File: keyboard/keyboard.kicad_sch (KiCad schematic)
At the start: 200 parts

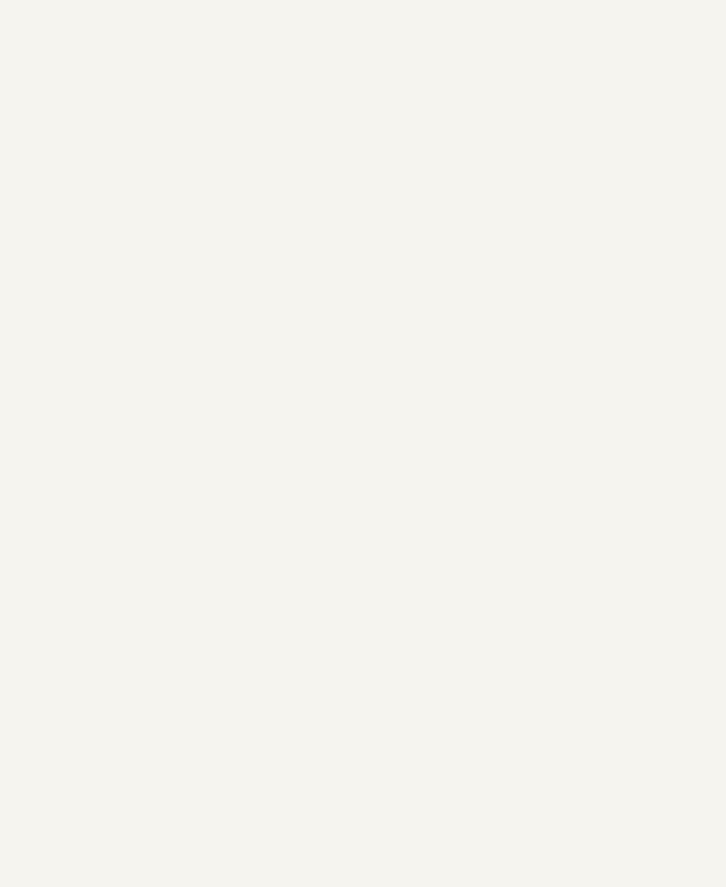
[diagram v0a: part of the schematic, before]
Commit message: Updated PCB with the Raspberry Pi Pico as MCU; connected all the rows and columns to the MCU
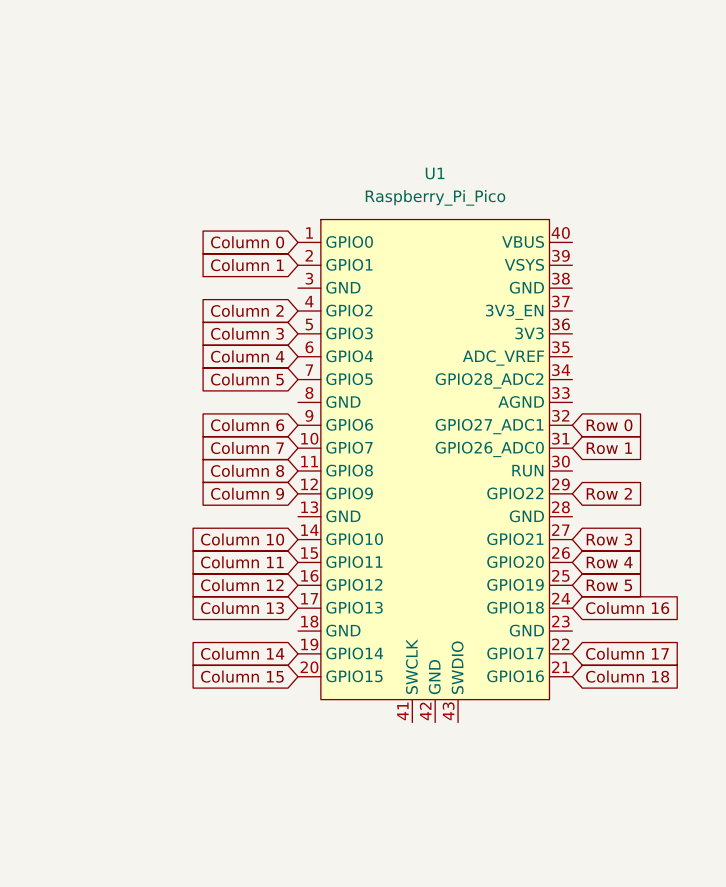
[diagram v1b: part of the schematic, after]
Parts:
- added U1: Raspberry_Pi_Pico, ScottoKeebs_MCU:Raspberry_Pi_Pico, symbol ScottoKeebs:MCU_Raspberry_Pi_Pico
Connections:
- net Column 0: now also U1.1 (GPIO0)
- net Column 1: now also U1.2 (GPIO1)
- net Column 10: now also U1.14 (GPIO10)
- net Column 11: now also U1.15 (GPIO11)
- net Column 12: now also U1.16 (GPIO12)
- net Column 13: now also U1.17 (GPIO13)
- net Column 14: now also U1.19 (GPIO14)
- net Column 15: now also U1.20 (GPIO15)
- net Column 16: now also U1.24 (GPIO18)
- net Column 17: now also U1.22 (GPIO17)
- net Column 18: now also U1.21 (GPIO16)
- net Column 2: now also U1.4 (GPIO2)
- net Column 3: now also U1.5 (GPIO3)
- net Column 4: now also U1.6 (GPIO4)
- net Column 5: now also U1.7 (GPIO5)
- net Column 6: now also U1.9 (GPIO6)
- net Column 7: now also U1.10 (GPIO7)
- net Column 8: now also U1.11 (GPIO8)
- net Column 9: now also U1.12 (GPIO9)
- net Row 0: now also U1.32 (GPIO27_ADC1)
- net Row 1: now also U1.31 (GPIO26_ADC0)
- net Row 2: now also U1.29 (GPIO22)
- net Row 3: now also U1.27 (GPIO21)
- net Row 4: now also U1.26 (GPIO20)
- net Row 5: now also U1.25 (GPIO19)
